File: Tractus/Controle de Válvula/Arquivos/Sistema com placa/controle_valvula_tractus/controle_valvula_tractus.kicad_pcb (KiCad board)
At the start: 2 copper layers, 52 x 68 mm, 42 parts, among them J1 Conn_02x04_Top_Bottom, J2 Conn_02x02_Top_Bottom, U1 R7FA4M1AB3CFM_AA0

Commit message: Alteração de arquivos do esquemático e pcb
Alteração de arquivos do esquemático e pcb
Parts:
- removed the REF** at (54.0, 124.0)
- removed the REF** at (54.0, 64.0)
- removed the REF** at (98.0, 64.0)
- removed the REF** at (98.0, 124.1)
- added REF**: MountingHole_3.5mm, MountingHole:MountingHole_3.5mm, F.Cu at (54.0, 64.0)
- added REF**: MountingHole_3.5mm, MountingHole:MountingHole_3.5mm, F.Cu at (98.0, 64.0)
- added REF**: MountingHole_3.5mm, MountingHole:MountingHole_3.5mm, F.Cu at (98.0, 124.0)
- added REF**: MountingHole_3.5mm, MountingHole:MountingHole_3.5mm, F.Cu at (54.0, 124.0)
- renumbered C9 to C10, C10 to C11, C11 to C6, C6 to C7, C7 to C8, C8 to C9, J1 to DISPLAY1, J2 to FONTE|VALVULA1, R7 to R10, R8 to R11, R9 to R12, R10 to R13, R11 to R14, R12 to R15, R13 to R16, R16 to R2, R15 to R3, R2 to R4, R14 to R5, R3 to R6, R4 to R7, R5 to R8, R6 to R9
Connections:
- RESET1 pad 2: unconnected-(RESET1-Pad2) -> GND

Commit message: Adding Files from e² studio
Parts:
- added C12: 1uF, Capacitor_SMD:C_1206_3216Metric, B.Cu at (66.4, 88.3)
- added R17: 10K, Resistor_SMD:R_1206_3216Metric, B.Cu at (68.8, 88.3)
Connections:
- AMP1 pad 3: /AMPOP_I -> Net-(AMP1A-+)
- U1 pad 51: unconnected-(U1-P502-Pad51) -> /AMPOP_I
- U1 pad 53: /AMPOP_I -> unconnected-(U1-P014-Pad53)
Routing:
- net /AMP1_O: track 65.1 -> 39.1 mm, vias 0 -> 1
- net +3.3V: track 175.7 -> 162.1 mm, vias 0 -> 1
- net Net-(AMP1A-+): track 0.00 -> 6.44 mm, vias 0 -> 1
- net /AMPOP_I: track 9.29 -> 3.38 mm, vias 0 -> 1
- net Net-(U1-P201/MD): track 38.0 -> 33.0 mm, vias 0 -> 2
- net +12V: track 61.8 -> 65.8 mm
- net GND: track 29.7 -> 31.4 mm

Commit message: Add op-amp decoupling and Uno PWM test
Updates the KiCad design to add C13 (100nF) and C14 (10uF) decoupling on the +12V rail near the op-amp section, with related schematic wiring, PCB routing, and reference updates. In the PlatformIO project, switches target from Uno R4 Minima to classic Uno, marks pioarduino as unwanted in VS Code recommendations, and replaces the previous LCD/flow-control sketch with a simple potentiometer-to-PWM output test program with serial monitoring.
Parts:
- added C13: 100nF, Capacitor_SMD:C_1206_3216Metric, F.Cu at (94.9, 81.4)
- added C14: 10uF, Capacitor_SMD:C_1206_3216Metric, F.Cu at (94.9, 84.7)
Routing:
- net +12V: track 65.8 -> 78.9 mm

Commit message: Atualizado diagrama da pcb
Mudanças para tornar o design mais organizado e limpo
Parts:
- C1, C3, C5, C7: footprint Capacitor_SMD:C_0805_2012Metric -> Capacitor_SMD:C_0603_1608Metric; moved to B.Cu
- C10: footprint Capacitor_SMD:C_1206_3216Metric -> Capacitor_SMD:C_0805_2012Metric
- C12, C13: footprint Capacitor_SMD:C_1206_3216Metric -> Capacitor_SMD:C_0603_1608Metric
- C2, C4: footprint Capacitor_SMD:C_1206_3216Metric -> Capacitor_SMD:C_0603_1608Metric; moved to B.Cu
- C6: footprint Capacitor_SMD:C_0805_2012Metric -> Capacitor_SMD:C_0603_1608Metric; moved to F.Cu
- C8: value 100nF -> 10uF
- C9: value 10uF -> 100nF; footprint Capacitor_SMD:C_1206_3216Metric -> Capacitor_SMD:C_0603_1608Metric
- R1, R16, R4, R6, R7, R8: footprint Resistor_SMD:R_1206_3216Metric -> Resistor_SMD:R_0603_1608Metric; moved to B.Cu
- R10, R11, R12, R13, R14, R15, R17, R9: footprint Resistor_SMD:R_1206_3216Metric -> Resistor_SMD:R_0603_1608Metric
- R2, R3, R5: footprint Resistor_SMD:R_1206_3216Metric -> Resistor_SMD:R_0603_1608Metric; moved to F.Cu
- moved FONTE|VALVULA1 35.0 mm to (63.0, 97.7), turned to 180 degrees
- moved C14 27.7 mm to (67.5, 88.8), turned to 90 degrees
- moved C13 26.6 mm to (69.6, 89.6), turned to 90 degrees
- moved REG1 24.9 mm to (74.5, 95.4), turned to -90 degrees
- moved R9 24.7 mm to (76.3, 102.0)
- moved C12 23.5 mm to (82.3, 105.5)
- moved AMP1 23.4 mm to (81.7, 103.1)
- moved R6 23.1 mm to (80.7, 100.6), turned to 90 degrees
- moved C8 22.4 mm to (71.9, 89.2)
- moved R14 21.3 mm to (87.3, 102.7)
- moved R17 21.0 mm to (80.8, 105.5)
- moved C9 21.0 mm to (73.7, 89.4), turned to 90 degrees
- moved REF** 20.7 mm to (98.2, 84.7)
- moved R15 20.7 mm to (86.5, 100.2), turned to -90 degrees
- moved REF** 20.7 mm to (53.8, 84.7)
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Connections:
- R11 pad 1: Net-(RGB1-Pin_1) -> Net-(RGB1-Pin_4)
- RGB1 pad 1: Net-(RGB1-Pin_1) -> GND
- RGB1 pad 4: GND -> Net-(RGB1-Pin_4)
- U1 pad 13: /BLUE -> /GREEN
- U1 pad 14: /GREEN -> /BLUE
- YF-B1|POT1 pad 1: GND -> /SENSOR_O
- YF-B1|POT1 pad 2: /POT_O -> +12V
- YF-B1|POT1 pad 3: +12V -> /POT_O
- YF-B1|POT1 pad 6: /SENSOR_O -> GND
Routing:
- net +3.3V: track 162.1 -> 107.7 mm, vias 1 -> 5
- net GND: track 31.4 -> 0.00 mm, vias 7 -> 0
- net +12V: track 78.9 -> 51.7 mm, vias 1 -> 0
- net /AMP1_O: track 39.1 -> 23.9 mm, vias 1 -> 0
- net Net-(U1-P201/MD): track 33.0 -> 18.6 mm, vias 2 -> 1
- net /POT_O: track 13.3 -> 0.00 mm
- net /USB_D+: track 18.1 -> 6.29 mm
- net /USB_D-: track 18.2 -> 6.43 mm
- net /SENSOR_O: track 19.0 -> 7.91 mm
- net /TFT_RST: track 30.4 -> 21.0 mm
- net Net-(U1-VCC_USB_LDO): track 12.2 -> 2.97 mm, vias 0 -> 1
- net /TFT_CS: track 23.1 -> 15.0 mm
- net /TFT_DC: track 26.8 -> 18.9 mm
- net /BLUE: track 11.3 -> 3.55 mm
- net /SPI_MOSI: track 19.4 -> 11.9 mm
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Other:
- board size 52 x 68 mm -> 52 x 53.4 mm

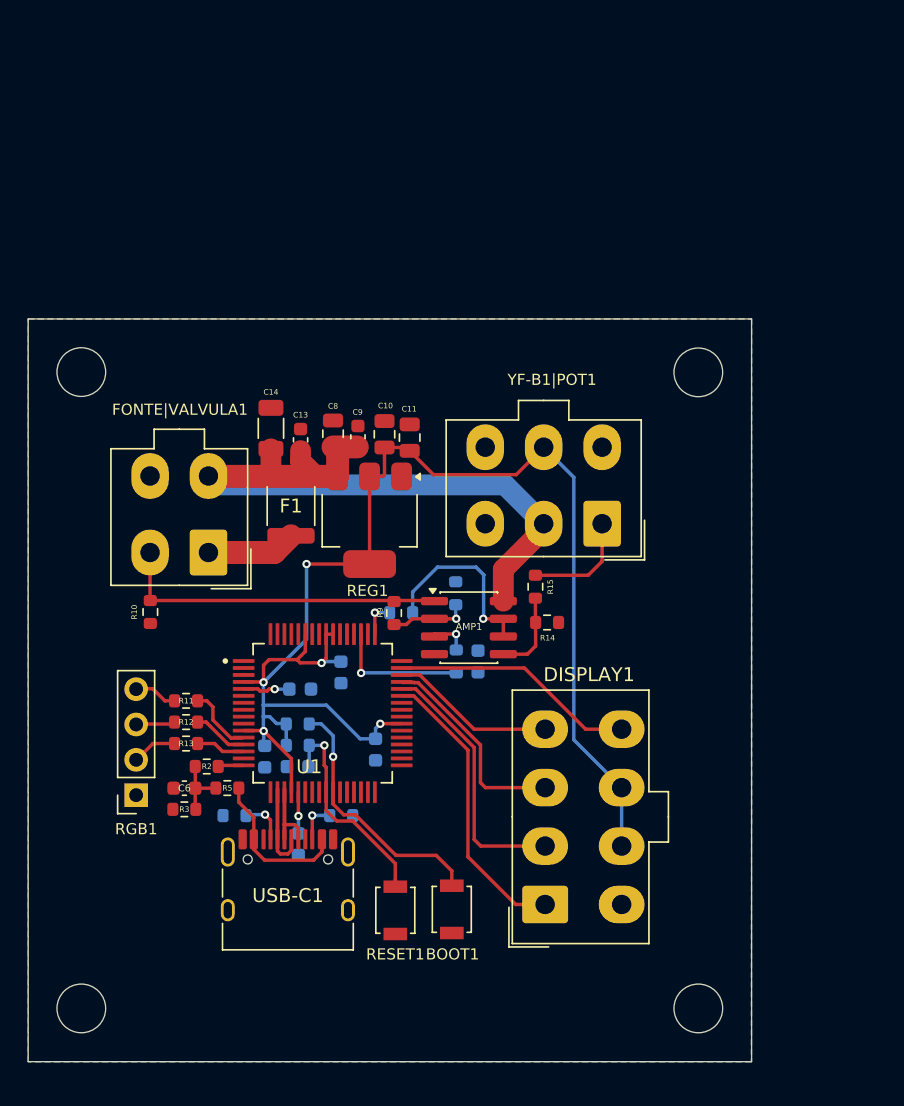
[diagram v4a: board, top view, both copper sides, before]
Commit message: Adicionado circuito de failsafe para fechamento da válvula
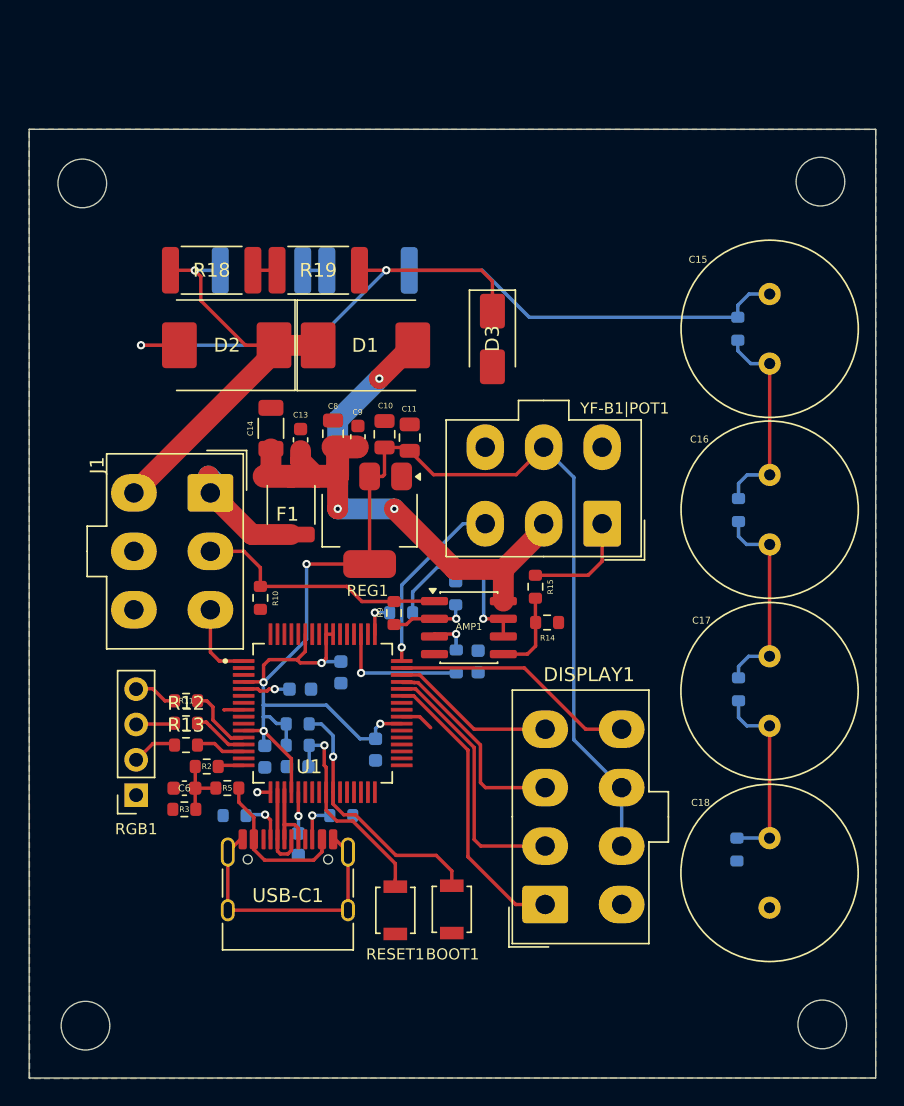
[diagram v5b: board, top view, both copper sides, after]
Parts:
- removed FONTE|VALVULA1: Conn_02x02_Top_Bottom, Connector_Molex:Molex_Mini-Fit_Jr_5566-04A_2x02_P4.20mm_Vertical
- added C15: 4.7F, Capacitor_THT:C_Radial_D12.5mm_H20.0mm_P5.00mm, F.Cu at (103.3, 79.1)
- added C16: 4.7F, Capacitor_THT:C_Radial_D12.5mm_H20.0mm_P5.00mm, F.Cu at (103.3, 92.1)
- added C17: 4.7F, Capacitor_THT:C_Radial_D12.5mm_H20.0mm_P5.00mm, F.Cu at (103.3, 105.2)
- added C18: 4.7F, Capacitor_THT:C_Radial_D12.5mm_H20.0mm_P5.00mm, F.Cu at (103.3, 118.2)
- added D1: D_Schottky, Diode_SMD:D_SMC, F.Cu at (74.2, 82.8)
- added D2: D_Schottky, Diode_SMD:D_SMC, F.Cu at (64.3, 82.8)
- added D3: D_Zener, Diode_SMD:D_SMA, F.Cu at (83.4, 82.3)
- added J1: FONTE|VALVE, Connector_Molex:Molex_Mini-Fit_Jr_5566-06A_2x03_P4.20mm_Vertical, F.Cu at (63.1, 93.4)
- added R18: 20, Resistor_SMD:R_2512_6332Metric, F.Cu at (63.2, 77.4)
- added R19: 20, Resistor_SMD:R_2512_6332Metric, F.Cu at (70.8, 77.4)
- added R20: 10K, Resistor_SMD:R_0603_1608Metric, B.Cu at (101.0, 81.6)
- added R21: 10K, Resistor_SMD:R_0603_1608Metric, B.Cu at (101.1, 94.6)
- added R22: 10K, Resistor_SMD:R_0603_1608Metric, B.Cu at (101.1, 107.5)
- added R23: 10K, Resistor_SMD:R_0603_1608Metric, B.Cu at (101.0, 119.0)
- added R24: 20, Resistor_SMD:R_2512_6332Metric, B.Cu at (66.8, 77.4)
- added R25: 20, Resistor_SMD:R_2512_6332Metric, B.Cu at (74.4, 77.4)
- moved REF** 16.3 mm to (107.0, 71.0)
- moved REF** 13.6 mm to (53.9, 71.2)
- moved REF** 8.98 mm to (107.1, 131.6)
- moved R10 7.97 mm to (66.7, 101.0)
- moved REF** 1.28 mm to (54.1, 131.7)
- moved R13 0.11 mm to (61.3, 111.5)
- moved F1 0.09 mm to (68.9, 94.3)
- moved R12 0.08 mm to (61.3, 110.0)
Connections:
- R12 pad 1: Net-(RGB1-Pin_2) -> Net-(RGB1-Pin_3)
- R13 pad 1: Net-(RGB1-Pin_3) -> Net-(RGB1-Pin_2)
- U1 pad 1: unconnected-(U1-P400-Pad1) -> /VALVE_FB
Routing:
- net Net-(D2-A): track 0.00 -> 64.8 mm, vias 0 -> 2
- net +12V - Valve: track 0.00 -> 30.5 mm, vias 0 -> 1
- net GND: track 0.00 -> 24.7 mm, vias 0 -> 1
- net Net-(C15-Pad2): track 0.00 -> 15.0 mm
- net Net-(C16-Pad2): track 0.00 -> 14.9 mm
- net Net-(C17-Pad2): track 0.00 -> 14.1 mm
- net /POT_O: track 0.00 -> 13.3 mm, vias 0 -> 1
- net /VALVE_FB: track 0.00 -> 5.70 mm
- net /AMP1_O: track 23.9 -> 18.5 mm
- net Net-(R24-Pad2): track 0.00 -> 1.73 mm
- net Net-(R18-Pad2): track 0.00 -> 1.73 mm
- net +12Vi: track 6.43 -> 7.98 mm
- net +12V: track 51.7 -> 52.2 mm, vias 0 -> 3
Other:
- board size 52 x 53.4 mm -> 60.9 x 68.2 mm
